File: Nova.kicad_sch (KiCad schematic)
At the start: 37 parts, among them J1 MEM2067-02-180-00-A, J2 Breakout, J3 Probe, Q1 2N7002, Q2 BC817, SW1 PTS636 SK25J, U1 STM32L552RCT6, U2 W25N01GVZEIG, U3 FM24CL16B, Y1 ECS-160-9-33B-CTP-TR, Y2 ECS-.327-9-12R-TR

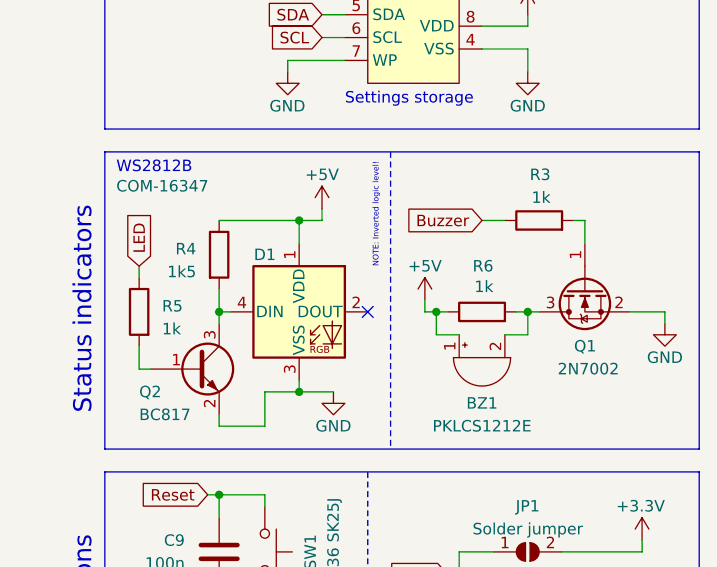
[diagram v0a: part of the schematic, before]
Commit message: :building_construction: Simplify power circuit and consolidate BOM
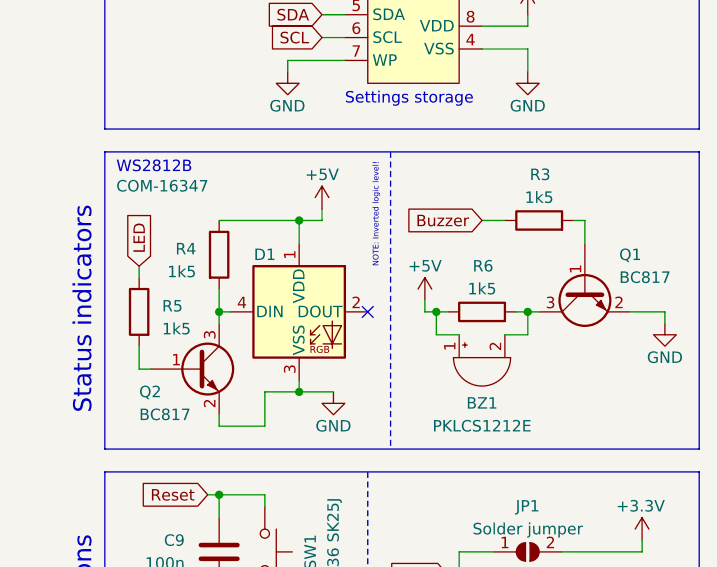
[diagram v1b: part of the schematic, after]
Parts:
- removed Q1: 2N7002, Package_TO_SOT_SMD:SOT-23, symbol Transistor_FET:2N7002
- added Q1: BC817, Package_TO_SOT_SMD:SOT-23, symbol Transistor_BJT:BC817
- R3, R5, R6: value 1k -> 1k5
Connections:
- net GND: now also Q1.2 (E)
- net at BZ1.2 (+), R6.2: now also Q1.3 (C)
- net at R3.2: now also Q1.1 (B)
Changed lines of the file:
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@@
+    )
+  )
+  (symbol (lib_id "Transistor_BJT:BC817") (at 270.51 120.65 90) (mirror x) (unit 1)
+    (in_bom yes) (on_board yes) (dnp no)
+    (property "Reference" "Q1" (at 274.32 116.84 90)
+      (effects (font (size 1.27 1.27)) (justify right))
+    )
+    (property "Value" "BC817" (at 274.32 119.38 90)
+      (effects (font (size 1.27 1.27)) (justify right))
+    )
+    (property "Footprint" "Package_TO_SOT_SMD:SOT-23" (at 272.415 125.73 0)
+      (effects (font (size 1.27 1.27) italic) (justify left) hide)
+    )
+    (property "Datasheet" "https://www.onsemi.com/pub/Collateral/BC818-D.pdf" (at 270.51 120.65 0)
+      (effects (font (size 1.27 1.27)) (justify left) hide)
+    )
+    (pin "1")
+    (pin "2")
+    (pin "3")
+    (instances
+      (project "Nova"
+        (path "/0c006d9f-ae30-49aa-ab15-ff0bec4de0e8"
+          (reference "Q1") (unit 1)
+        )
+      )
     )
   )
@@
       (effects (font (size 1.27 1.27)) (justify right))
     )
-    (property "Value" "1k" (at 223.52 125.095 0)
+    (property "Value" "1k5" (at 223.52 125.095 0)
       (effects (font (size 1.27 1.27)) (justify right))
     )
@@
       (effects (font (size 1.27 1.27)) (justify left))
     )
-    (property "Value" "1k" (at 266.7 110.49 90)
-      (effects (font (size 1.27 1.27)) (justify left))
+    (property "Value" "1k5" (at 265.43 110.49 90)
+      (effects (font (size 1.27 1.27)))
     )
     (property "Footprint" "Resistor_SMD:R_0402_1005Metric_Pad0.72x0.64mm_HandSolder" (at 265.43 114.808 90)
@@
       (effects (font (size 1.27 1.27)) (justify left))
     )
-    (property "Value" "1k" (at 260.3499 120.396 90)
-      (effects (font (size 1.27 1.27)) (justify left))
+    (property "Value" "1k5" (at 259.08 120.65 90)
+      (effects (font (size 1.27 1.27)))
     )
     (property "Footprint" "Resistor_SMD:R_0402_1005Metric_Pad0.72x0.64mm_HandSolder" (at 259.08 124.968 90)
@@
         )
       )
-    )
-  )
-  (symbol (lib_id "Transistor_FET:2N7002") (at 270.51 120.65 90) (mirror x) (unit 1)
-    (in_bom yes) (on_board yes) (dnp no)
-    (property "Reference" "Q1" (at 271.78 127 90)
-      (effects (font (size 1.27 1.27)) (justify left))
-    )
-    (property "Value" "2N7002" (at 274.32 129.54 90)
-      (effects (font (size 1.27 1.27)) (justify left))
-    )
-    (property "Footprint" "Package_TO_SOT_SMD:SOT-23" (at 272.415 125.73 0)
-      (effects (font (size 1.27 1.27) italic) (justify left) hide)
-    )
-    (property "Datasheet" "https://www.onsemi.com/pub/Collateral/NDS7002A-D.PDF" (at 270.51 120.65 0)
-      (effects (font (size 1.27 1.27)) (justify left) hide)
-    )
-    (pin "1")
-    (pin "2")
-    (pin "3")
-    (instances
-      (project "Nova"
-        (path "/0c006d9f-ae30-49aa-ab15-ff0bec4de0e8"
-          (reference "Q1") (unit 1)
-        )
-      )

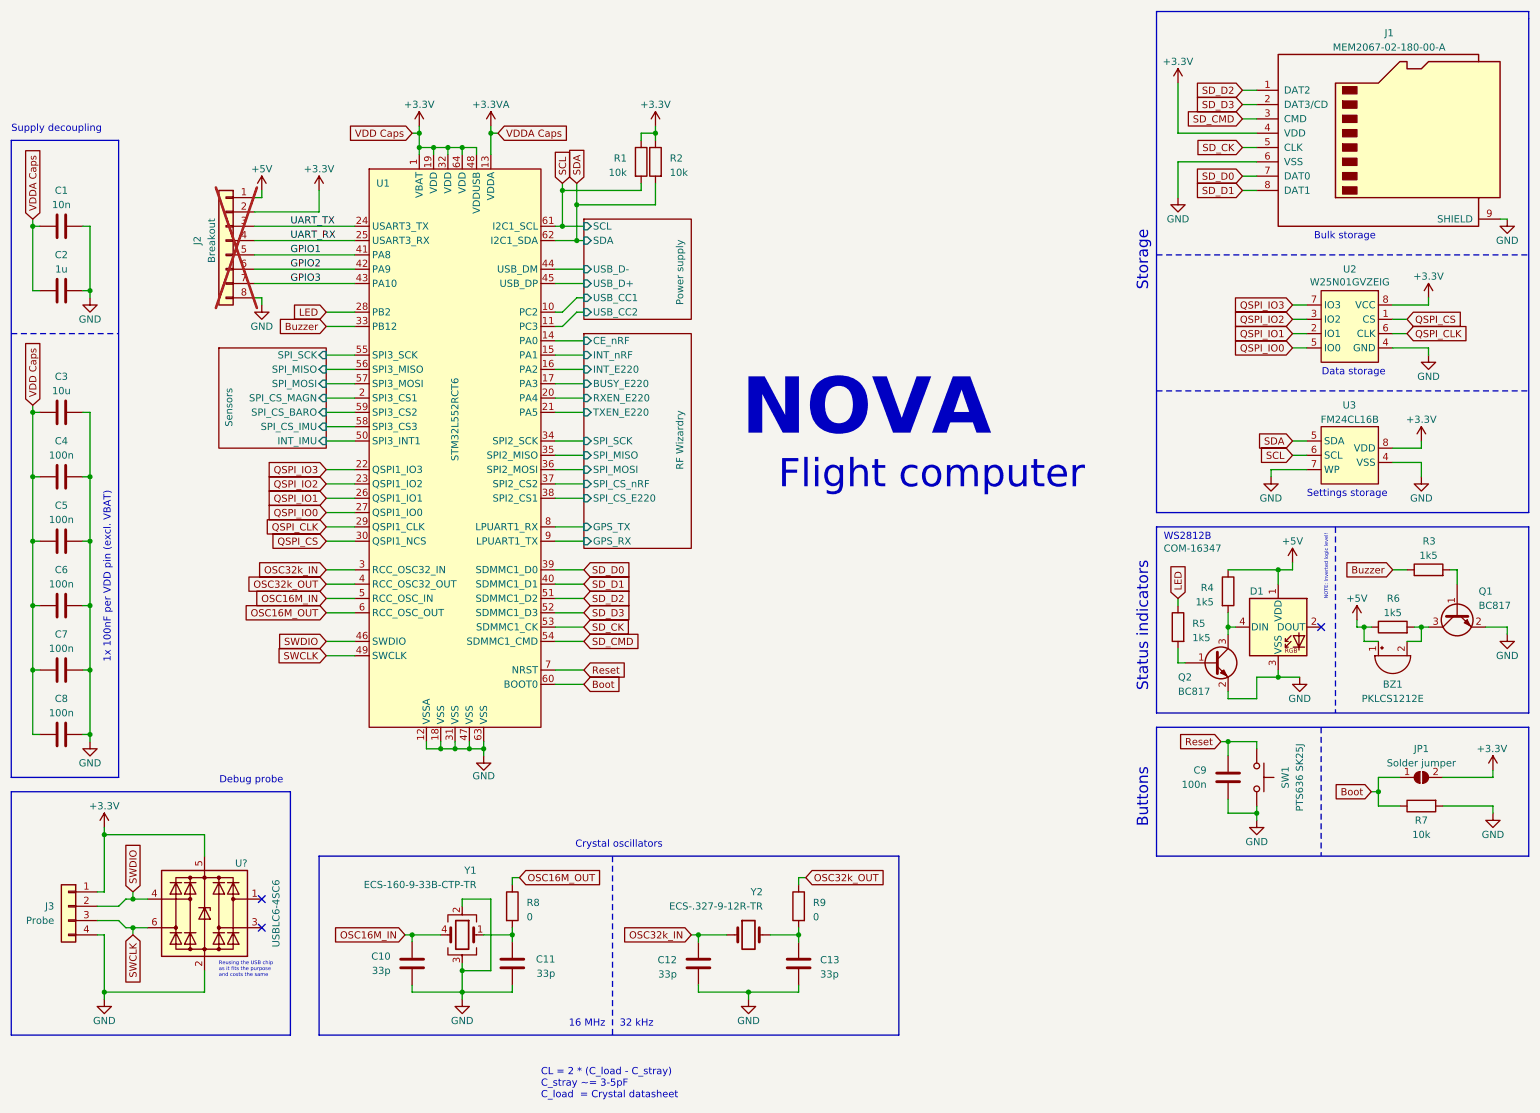
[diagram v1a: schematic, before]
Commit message: :building_construction: Replace debug header with TagConnect and inline STM32 decoupling caps
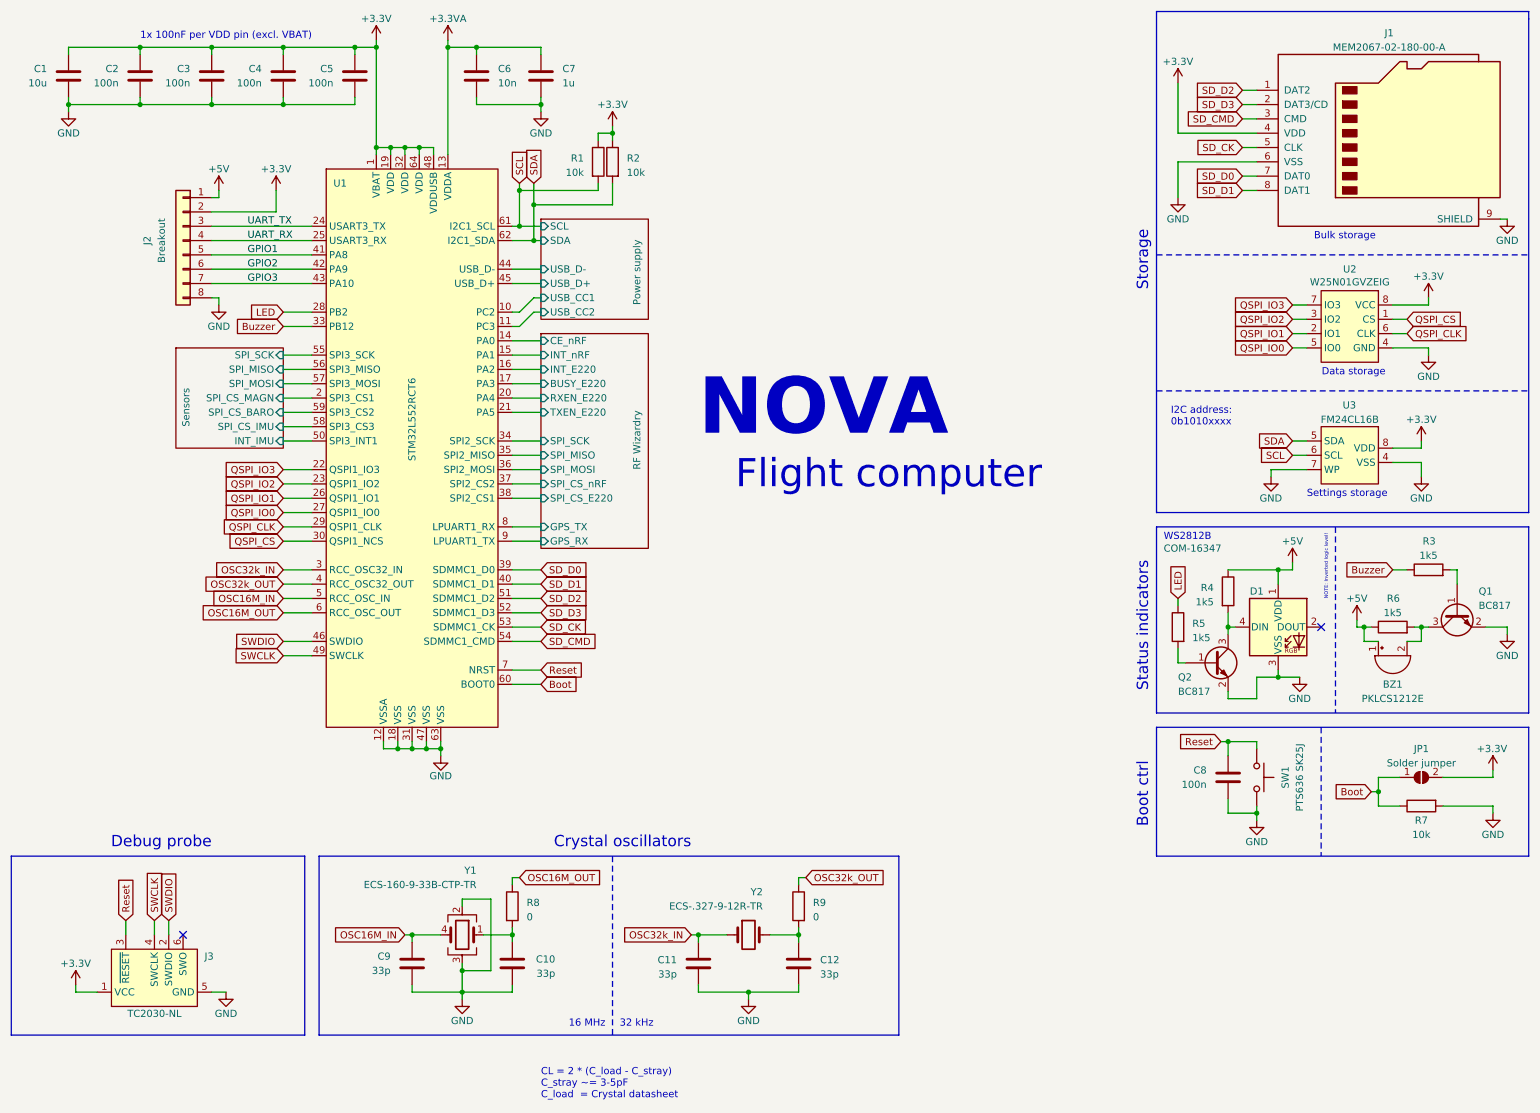
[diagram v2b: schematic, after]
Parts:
- removed C8: 100n, Capacitor_SMD:C_0402_1005Metric_Pad0.74x0.62mm_HandSolder, symbol Device:C
- removed J3: Probe, Connector_PinHeader_2.54mm:PinHeader_1x04_P2.54mm_Vertical, symbol Connector_Generic:Conn_01x04
- removed U?: USBLC6-4SC6, Package_TO_SOT_SMD:SOT-23-6, symbol Power_Protection:USBLC6-4SC6
- added J3: TC2030-NL, Connector:Tag-Connect_TC2030-IDC-NL_2x03_P1.27mm_Vertical, symbol Connector:Conn_ARM_SWD_TagConnect_TC2030-NL
- C1: value 10n -> 10u; footprint Capacitor_SMD:C_0402_1005Metric_Pad0.74x0.62mm_HandSolder -> Capacitor_SMD:C_0603_1608Metric_Pad1.08x0.95mm_HandSolder
- C2: value 1u -> 100n; footprint Capacitor_SMD:C_0603_1608Metric_Pad1.08x0.95mm_HandSolder -> Capacitor_SMD:C_0402_1005Metric_Pad0.74x0.62mm_HandSolder
- C3: value 10u -> 100n; footprint Capacitor_SMD:C_0603_1608Metric_Pad1.08x0.95mm_HandSolder -> Capacitor_SMD:C_0402_1005Metric_Pad0.74x0.62mm_HandSolder
- C6: value 100n -> 10n
- C7: value 100n -> 1u; footprint Capacitor_SMD:C_0402_1005Metric_Pad0.74x0.62mm_HandSolder -> Capacitor_SMD:C_0603_1608Metric_Pad1.08x0.95mm_HandSolder
- J2: now fitted
- renumbered C11 to C10, C12 to C11, C13 to C12, C9 to C8, C10 to C9
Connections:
- net +3.3V: now also C1.2, C2.2, C3.2, C4.2, C5.2, J3.1 (VCC); no longer C3.1, C4.1, C5.1, C6.1, C7.1
- net +3.3VA: now also C6.2, C7.1; no longer C1.1, C2.1
- net GND: now also C1.1, C2.1, C3.1, C4.1, C5.1, C6.1, J3.5 (GND); no longer C1.2, C2.2, C3.2, C4.2, C5.2, C6.2
- net Reset: now also J3.3 (~{RESET})
- net SWCLK: now also J3.4 (SWCLK)
- net SWDIO: now also J3.2 (SWDIO)
- no-connect marks 3 -> 2
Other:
- note added: "Boot ctrl"
- note added: "I2C address: 0b1010xxxx"
- note removed: "Buttons"
- note removed: "Reusing the USB chip as it fits the purpose and costs the same"
- note removed: "Supply decoupling"
- moved on the sheet: R1, R2, U1
